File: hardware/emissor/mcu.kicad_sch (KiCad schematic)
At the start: 15 parts, among them J1 I2C, SW1 RESET, SW2 BOOT, U1 ESP32-C3-MINI-1-H4X

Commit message: feat(hw): placas emissor e receptor com layout posicionado, 3D e STEP (hw-v0.1 em andamento)
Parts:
- JP1: value PAPEL: fechar=BOMBA -> PAPEL=RESERV.
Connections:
- net FLOAT_LOW_PUMP_DRV renamed FLOAT_LOW
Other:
- note added: "Alimentacao 3V3 (3,0-3,6 V). EN com RC de 10 k + 1 uF (p.34). Strapping (Tabela 4-3, p.13): GPIO9=1 no boot (pull-up 4k7 + botao BOOT); GPIO8=1 para download (pull-up 4k7, tambem SDA); GPIO2 com pull-up (recomendado). GPIO18/19 = USB Serial/JTAG. GPIO20/21 = UART0 (console): ver decisoes.md."
- note removed: "Alimentacao 3V3 (3,0-3,6 V, Tabela 1 / p.1). EN com RC de 10 k + 1 uF (p.34). Strapping (Tabela 4-3, p.13): GPIO9=1 no boot (pull-up 4k7 + botao BOOT); GPIO8=1 para download (pull-up 4k7, tambem SDA); GPIO2 com pull-up (recomendado). GPIO18/19 = USB Serial/JTAG. GPIO20/21 = UART0 (console): ver decisoes.md."
- note removed: "TEMP: PWR_FLAG de +3V3 e GND saem quando a folha de alimentacao for criada."
- title: MCU: ESP32-C3-MINI-1 -> MCU - Emissor (reservatorio)

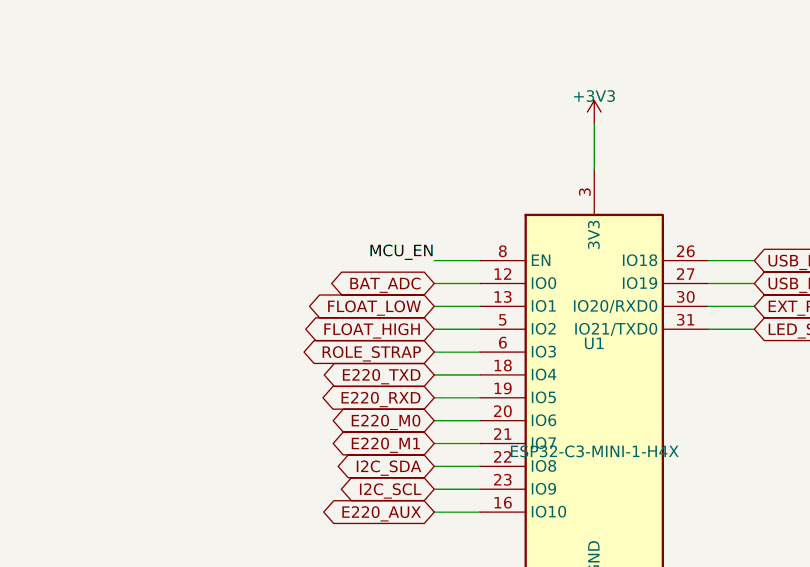
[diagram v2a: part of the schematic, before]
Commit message: feat(hw): jack 12 V com buck AP63205, roteador proprio e serigrafia padronizada (receptor roteado; emissor com 1 net aberta)
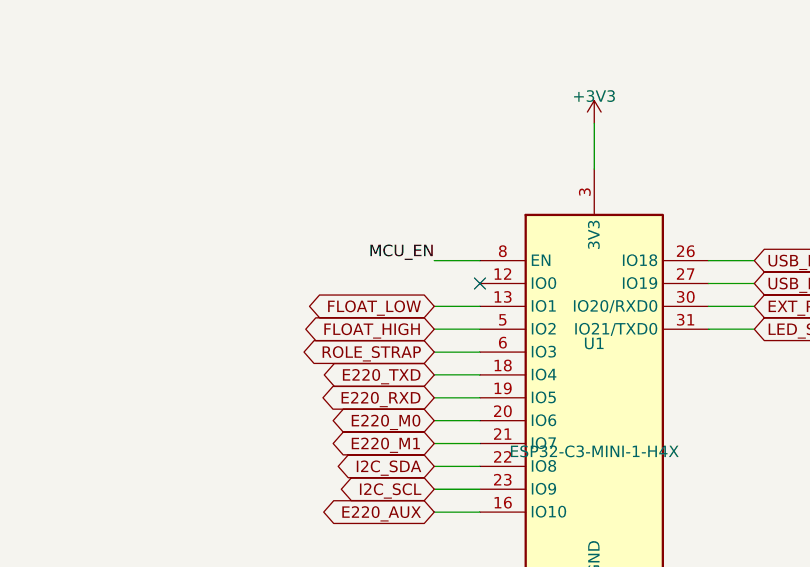
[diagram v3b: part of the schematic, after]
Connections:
- net BAT_ADC: no longer names the net of U1.12 (IO0)
- no-connect marks 0 -> 1
